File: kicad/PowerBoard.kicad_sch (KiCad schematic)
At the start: 147 parts, among them IC1 LT1910ES8#PBF, IC2 LT1910ES8#PBF, IC3 LT1910ES8#PBF, IC4 LT1910ES8#PBF, IC5 LT1910ES8#PBF, IC7 MAX17541GATB+T, J1 XT90, J10 XT90, J11 XT90, J12 XT90, J13 XT90, J14 DEAN_T, J15 DEAN_T, J16 DEAN_T, J17 DEAN_T, J18 DEAN_T, J19 DEAN_T, J2 DEAN_T, J20 XT60, J21 XT60, J22 XT60, J23 XT60, J24 XT60, J25 XT60, J26 XT60, J27 XT60, J28 XT60, J29 XT60, J3 XT60, J30 XT60, J31 XT60, J32 XT30, J33 XT30, J34 XT30, J35 XT30, J36 XT30, J37 XT30, J38 XT30, J39 XT30, J4 XT30, J40 XT30, J41 XT60, J5 Conn_01x02, J6 XT90, J7 XT90, J8 XT90, J9 XT90, Q1 IRFS7530TRL7PP, Q2 IRFS7437TRLPBF, Q3 IRFS7437TRLPBF, Q4 IRFS7437TRLPBF, Q5 IRFS7437TRLPBF, U1 Pico, U2 INA238, U3 INA238, U4 INA238, U5 INA238, U6 INA238

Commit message: Add first firmware version
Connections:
- net +42V: no longer D20.2 (A)
- net 42_SHUNT: now reaches Q1.4 (D), R1.4
- net 42_SHUNT: now also D20.2 (A)
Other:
- moved on the sheet: D20
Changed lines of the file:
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@@
 	)
 	(junction
-		(at 246.38 44.45)
-		(diameter 0)
-		(color 0 0 0 0)
-	)
-	(junction
 		(at 297.18 101.6)
 		(diameter 0)
@@
 	)
 	(junction
+		(at 38.1 71.12)
+		(diameter 0)
+		(color 0 0 0 0)
+	)
+	(junction
 		(at 93.98 234.95)
 		(diameter 0)
@@
 	)
 	(junction
+		(at 246.38 44.45)
+		(diameter 0)
+		(color 0 0 0 0)
+	)
+	(junction
 		(at 142.24 260.35)
 		(diameter 0)
@@
 	(wire
 		(pts
-			(xy 246.38 31.75) (xy 246.38 34.29)
+			(xy 238.76 36.83) (xy 246.38 36.83)
 		)
 		(stroke
@@
 	(wire
 		(pts
+			(xy 228.6 36.83) (xy 231.14 36.83)
+		)
+		(stroke
+			(width 0)
+			(type default)
+		)
+	)
+	(wire
+		(pts
 			(xy 245.11 120.65) (xy 252.73 120.65)
 		)
@@
 	(wire
 		(pts
-			(xy 246.38 41.91) (xy 246.38 44.45)
-		)
-		(stroke
-			(width 0)
-			(type default)
-		)
-	)
-	(wire
-		(pts
 			(xy 162.56 111.76) (xy 195.58 111.76)
 		)
@@
 	(wire
 		(pts
+			(xy 27.94 71.12) (xy 38.1 71.12)
+		)
+		(stroke
+			(width 0)
+			(type default)
+		)
+	)
+	(wire
+		(pts
 			(xy 118.11 234.95) (xy 118.11 241.3)
 		)
@@
 	(wire
 		(pts
-			(xy 242.57 44.45) (xy 242.57 33.02)
+			(xy 242.57 33.02) (xy 242.57 44.45)
 		)
 		(stroke
@@
 	(wire
 		(pts
+			(xy 246.38 36.83) (xy 246.38 44.45)
+		)
+		(stroke
+			(width 0)
+			(type default)
+		)
+	)
+	(wire
+		(pts
 			(xy 309.88 231.14) (xy 309.88 236.22)
 		)
@@
 	)
 	(rectangle
-		(start 19.05 21.59)
+		(start 13.97 21.59)
 		(end 113.03 86.36)
 		(stroke
@@
 	)
 	(rectangle
-		(start 218.44 21.59)
+		(start 214.63 21.59)
 		(end 332.74 81.28)
 		(stroke
@@
 	(text "5V AUX Switched Power Supply"
 		(exclude_from_sim no)
-		(at 249.428 24.638 0)
+		(at 246.126 24.638 0)
 		(effects
 			(font
@@
 		)
 	)
+	(global_label "42_SHUNT"
+		(shape input)
+		(at 27.94 71.12 180)
+		(fields_autoplaced yes)
+		(effects
+			(font
+				(size 1.27 1.27)
+			)
+			(justify right)
+		)
+		(property "Intersheetrefs" "${INTERSHEET_REFS}"
+			(at 15.3996 71.12 0)
+			(effects
+				(font
+					(size 1.27 1.27)
+				)
+				(justify right)
+				(hide yes)
+			)
+		)
+	)
 	(global_label "ALERT_5"
 		(shape input)
@@
 		)
 	)
+	(global_label "42_SHUNT"
+		(shape input)
+		(at 228.6 36.83 180)
+		(fields_autoplaced yes)
+		(effects
+			(font
+				(size 1.27 1.27)
+			)
+			(justify right)
+		)
+		(property "Intersheetrefs" "${INTERSHEET_REFS}"
+			(at 216.0596 36.83 0)
+			(effects
+				(font
+					(size 1.27 1.27)
+				)
+				(justify right)
+				(hide yes)
+			)
+		)
+	)
 	(global_label "24V_2"
 		(shape input)
@@
 	(symbol
 		(lib_id "Device:D")
-		(at 246.38 38.1 90)
+		(at 234.95 36.83 180)
 		(unit 1)
 		(exclude_from_sim no)
@@
 		(fields_autoplaced yes)
 		(property "Reference" "D20"
-			(at 248.92 36.8299 90)
+			(at 234.95 30.48 0)
 			(effects
 				(font
 					(size 1.27 1.27)
 				)
-				(justify right)
 			)
 		)
 		(property "Value" "D"
-			(at 248.92 39.3699 90)
+			(at 234.95 33.02 0)
 			(effects
 				(font
 					(size 1.27 1.27)
 				)
-				(justify right)
 			)
 		)
 		(property "Footprint" "Diode_SMD:D_1206_3216Metric"
-			(at 246.38 38.1 0)
+			(at 234.95 36.83 0)
 			(effects
 				(font
@@
 		)
 		(property "Datasheet" "~"
-			(at 246.38 38.1 0)
+			(at 234.95 36.83 0)
 			(effects
 				(font
@@
 		)
 		(property "Description" "Diode"
-			(at 246.38 38.1 0)
+			(at 234.95 36.83 0)
 			(effects
 				(font
@@
 		)
 		(property "Sim.Device" "D"
-			(at 246.38 38.1 0)
+			(at 234.95 36.83 0)
 			(effects
 				(font
@@
 		)
 		(property "Sim.Pins" "1=K 2=A"
-			(at 246.38 38.1 0)
+			(at 234.95 36.83 0)
 			(effects
 				(font
@@
 					(unit 1)
 				)
-			)
-		)
-	)
-	(symbol
-		(lib_id "power:+48V")
-		(at 246.38 31.75 0)
-		(unit 1)
-		(exclude_from_sim no)
-		(in_bom yes)
-		(on_board yes)
-		(dnp no)
-		(property "Reference" "#PWR023"
-			(at 246.38 35.56 0)
-			(effects
-				(font
-					(size 1.27 1.27)
-				)
-				(hide yes)
-			)
-		)
-		(property "Value" "+42V"
-			(at 243.84 26.67 0)
-			(effects
-				(font
-					(size 1.27 1.27)
-				)
-				(justify left)
-			)
-		)
-		(property "Footprint" ""
-			(at 246.38 31.75 0)
-			(effects
-				(font
-					(size 1.27 1.27)
-				)
-				(hide yes)
-			)
-		)
-		(property "Datasheet" ""
-			(at 246.38 31.75 0)
-			(effects
-				(font
-					(size 1.27 1.27)
-				)
-				(hide yes)
-			)
-		)
-		(property "Description" "Power symbol creates a global label with name \"+42V\""
-			(at 246.38 31.75 0)
-			(effects
-				(font
-					(size 1.27 1.27)
-				)
-				(hide yes)
-			)
-		)
-		(pin "1"
-		)
-		(instances
-			(project "PowerBoard"
-				(path "/0dc459cd-c845-409c-9d50-e420f03142d8"
-					(reference "#PWR023")
-					(unit 1)
-				)

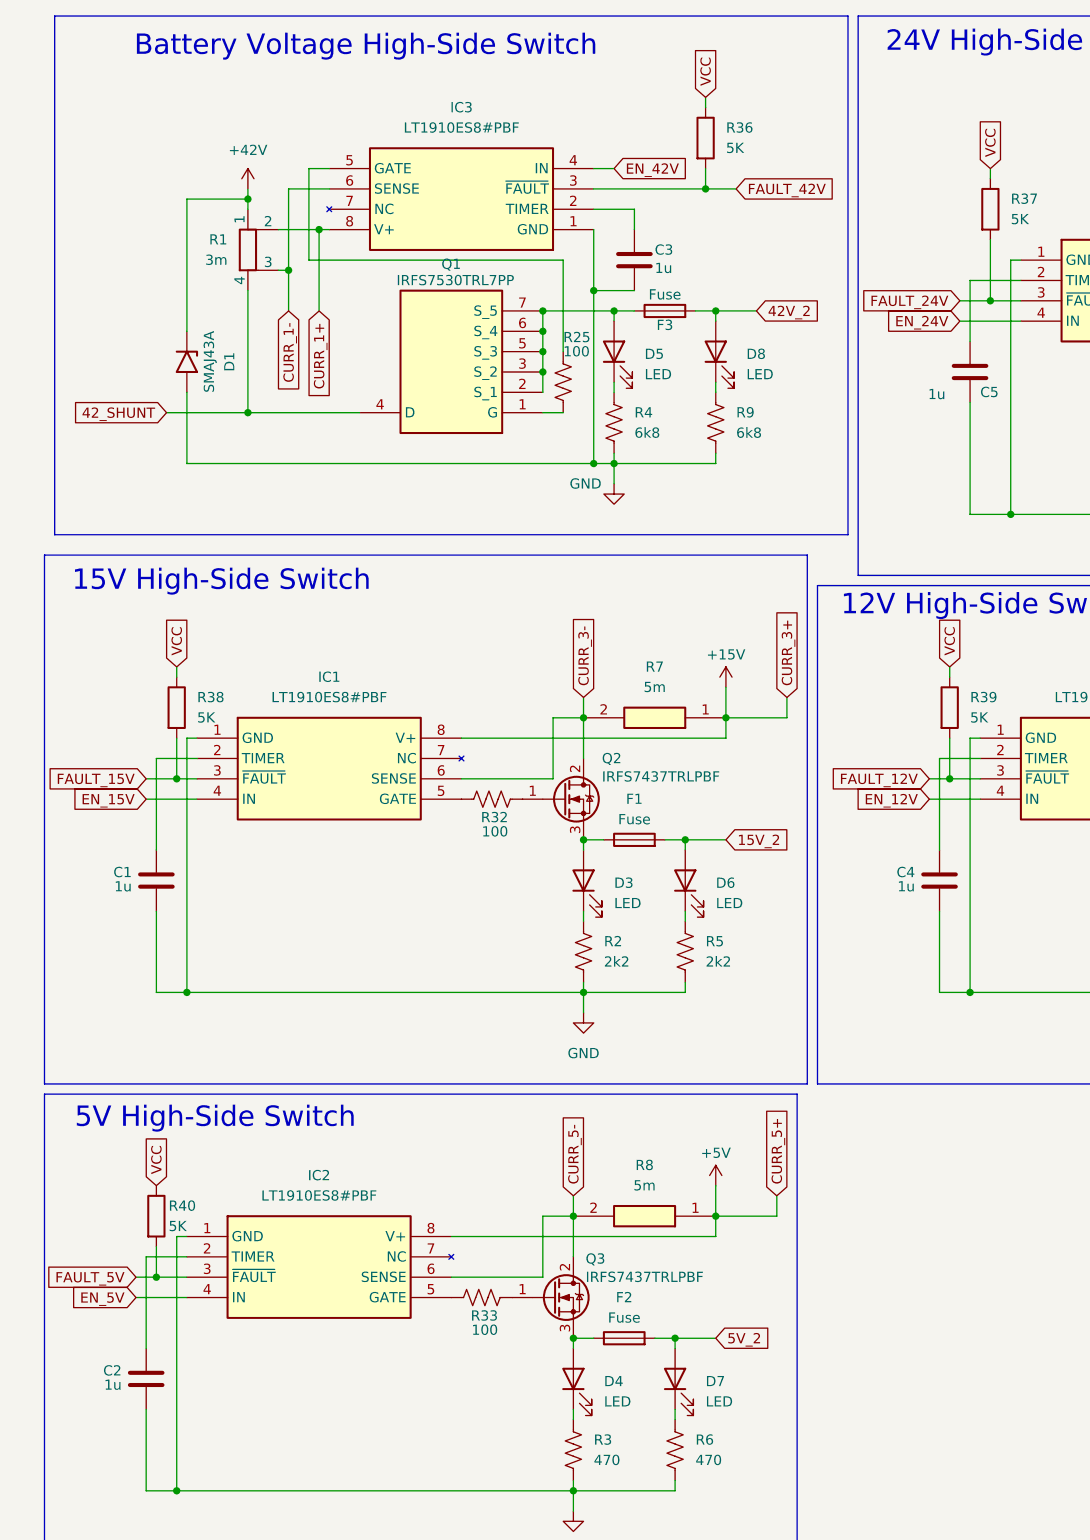
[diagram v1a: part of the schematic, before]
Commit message: Add dV/dt for inrush current limitation on the main power line
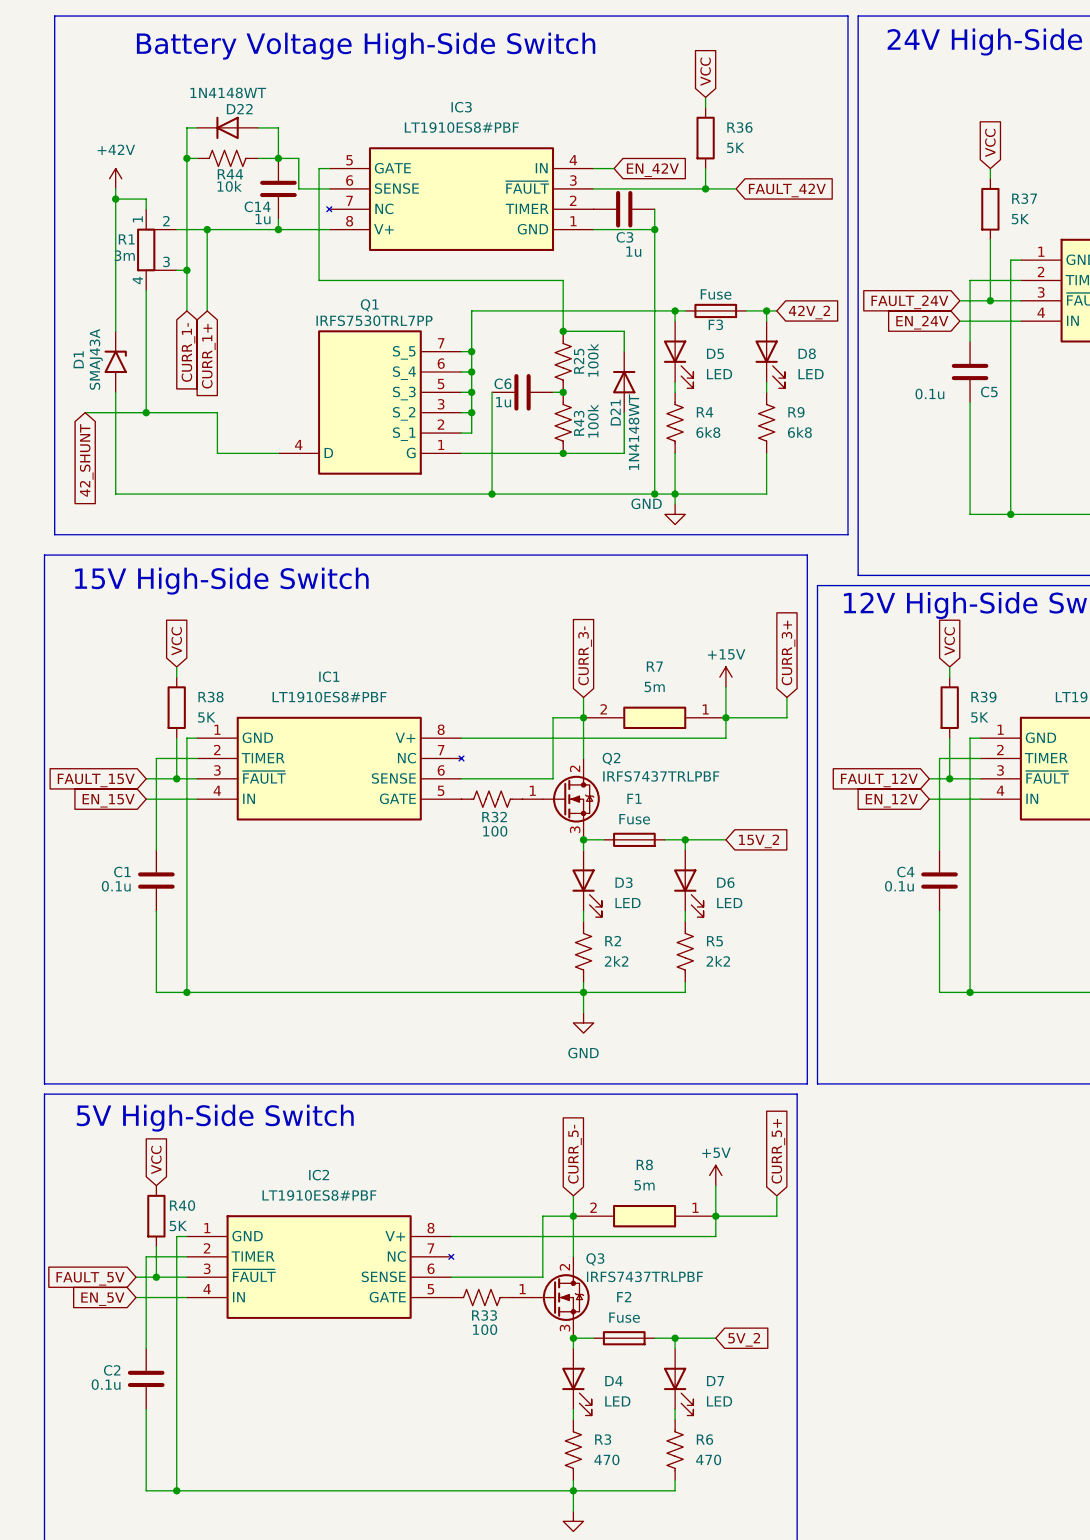
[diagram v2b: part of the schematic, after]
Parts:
- added C14, C6: 1u, Capacitor_SMD:C_0603_1608Metric, symbol Device:C
- added D21, D22: 1N4148WT, Diode_SMD:D_SOD-523, symbol Diode:1N4148WT
- added R43: 100k, Resistor_SMD:R_0603_1608Metric, symbol Device:R_US
- added R44: 10k, Resistor_SMD:R_0603_1608Metric, symbol Device:R_US
- C1, C2, C4, C5: value 1u -> 0.1u
- C10, C11, C12, C3, C7, C8, C9: footprint Capacitor_SMD:C_1206_3216Metric -> Capacitor_SMD:C_0603_1608Metric
- R16, R17, R21: footprint Resistor_SMD:R_1206_3216Metric -> Resistor_SMD:R_0603_1608Metric
- R25: value 100 -> 100k; footprint Resistor_SMD:R_1206_3216Metric -> Resistor_SMD:R_0603_1608Metric
- R4: footprint Resistor_SMD:R_1206_3216Metric -> Capacitor_SMD:C_0603_1608Metric
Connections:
- net CURR_1+: now also C14.2
- net CURR_1-: now also D22.1 (K), R44.1; no longer IC3.6 (SENSE)
- net GND: now also C6.1
- net at R25.1: now also C6.2, R43.1; no longer IC3.5 (GATE)
- net at Q1.1 (G): now also D21.2 (A), R43.2; no longer R25.2
- new net: D21.1 (K), IC3.5 (GATE), R25.2
- new net: C14.1, D22.2 (A), IC3.6 (SENSE), R44.2
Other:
- moved on the sheet: C3, D1, D5, D8, F3, Q1, R1, R25, R4, R9

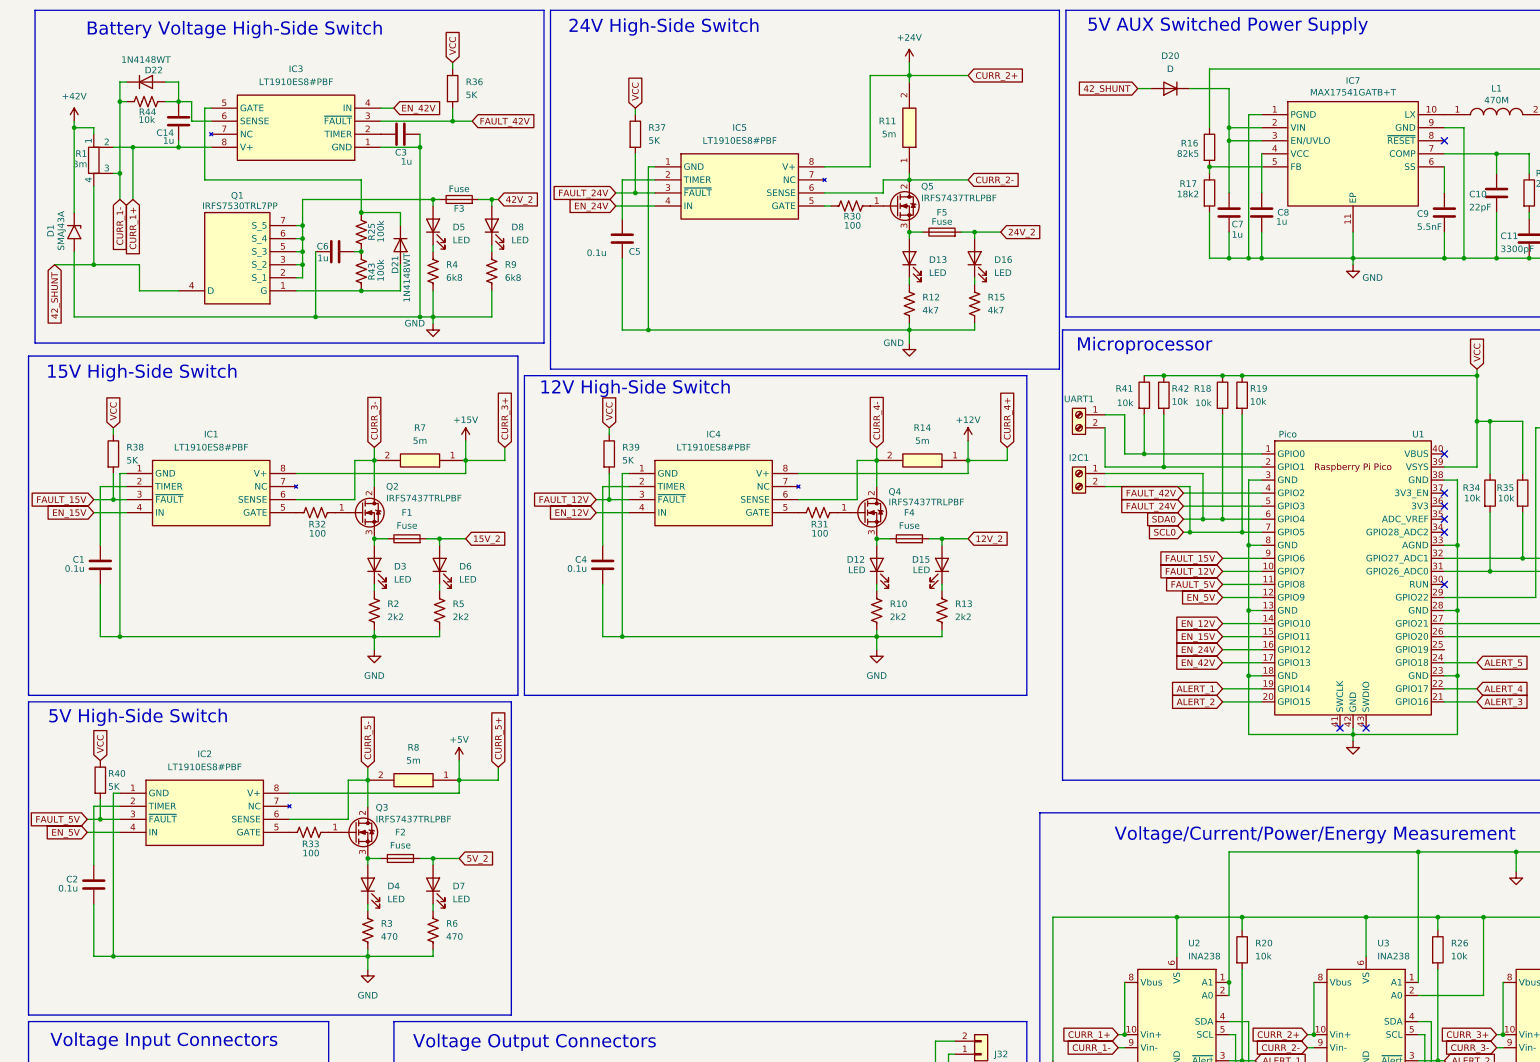
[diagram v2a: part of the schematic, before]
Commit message: finish inrush current limiting
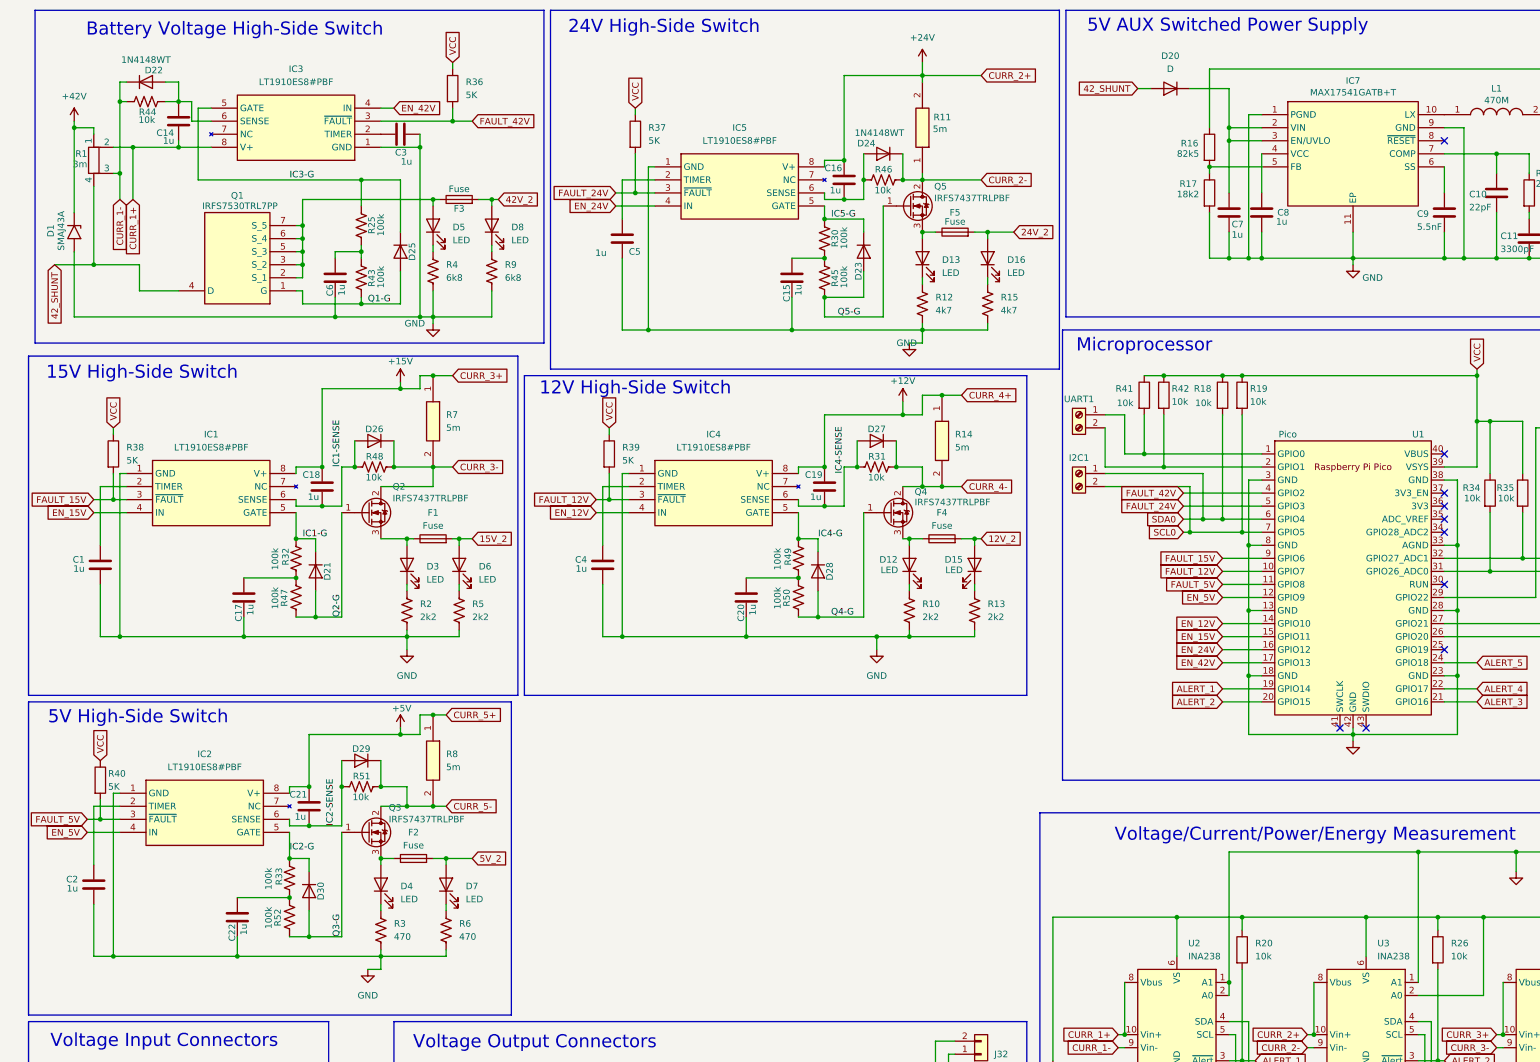
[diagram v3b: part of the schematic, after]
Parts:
- added C15, C16, C17, C18, C19, C20, C21, C22: 1u, Capacitor_SMD:C_0603_1608Metric, symbol Device:C
- added D23, D24, D25, D26, D27, D28, D29, D30: 1N4148WT, Diode_SMD:D_SOD-523, symbol Diode:1N4148WT
- added R45, R47, R49, R50, R52: 100k, Resistor_SMD:R_0603_1608Metric, symbol Device:R_US
- added R46, R48, R51: 10k, Resistor_SMD:R_0603_1608Metric, symbol Device:R_US
- C1, C2, C4, C5: value 0.1u -> 1u; footprint Capacitor_SMD:C_1206_3216Metric -> Capacitor_SMD:C_0603_1608Metric
- R10, R12, R2, R3: footprint Resistor_SMD:R_1206_3216Metric -> Resistor_SMD:R_0603_1608Metric
- R30, R32, R33: value 100 -> 100k; footprint Resistor_SMD:R_1206_3216Metric -> Resistor_SMD:R_0603_1608Metric
- R31: value 100 -> 10k; footprint Resistor_SMD:R_1206_3216Metric -> Resistor_SMD:R_0603_1608Metric
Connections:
- net +12V: now also C19.1
- net +15V: now also C18.1
- net +24V: now also C16.1
- net +5V: now also C21.1
- net CURR_2-: now also D24.1 (K), R46.2; no longer IC5.6 (SENSE)
- net CURR_3-: now also D26.1 (K), R48.2; no longer IC1.6 (SENSE)
- net CURR_4-: now also R31.2, D27.1 (K); no longer IC4.6 (SENSE)
- net CURR_5-: now also D29.1 (K), R51.2; no longer IC2.6 (SENSE)
- net GND: now also C15.1, C17.1, C20.1, C22.1
- net Q1-G: now reaches Q1.1 (G), R43.2
- net Q1-G: now also D25.2 (A); no longer D21.2 (A)
- net at R30.1: now also C15.2, R45.1; no longer IC5.5 (GATE)
- net IC5-G: now reaches R30.2
- net IC5-G: now also IC5.5 (GATE), D23.1 (K); no longer Q5.1 (G)
- net IC3-G: now reaches IC3.5 (GATE), R25.2
- net IC3-G: now also D25.1 (K); no longer D21.1 (K)
- net IC4-G: now reaches IC4.5 (GATE)
- net IC4-G: now also D28.1 (K), R49.2; no longer R31.1
- net IC1-G: now reaches R32.2
- net IC1-G: now also D21.1 (K), IC1.5 (GATE); no longer Q2.1 (G)
- net at R32.1: now also C17.2, R47.1; no longer IC1.5 (GATE)
- net Q4-G: now reaches Q4.1 (G)
- net Q4-G: now also D28.2 (A), R50.2; no longer R31.2
- net at R33.1: now also C22.2, R52.1; no longer IC2.5 (GATE)
- net IC2-G: now reaches R33.2
- net IC2-G: now also IC2.5 (GATE), D30.1 (K); no longer Q3.1 (G)
- new net: C20.2, R49.1, R50.1
- new net: C16.2, D24.2 (A), IC5.6 (SENSE), R46.1
- new net IC1-SENSE: C18.2, D26.2 (A), IC1.6 (SENSE), R48.1
- new net IC2-SENSE: C21.2, D29.2 (A), IC2.6 (SENSE), R51.1
- new net IC4-SENSE: C19.2, D27.2 (A), IC4.6 (SENSE), R31.1
- new net Q2-G: D21.2 (A), Q2.1 (G), R47.2
- new net Q3-G: D30.2 (A), Q3.1 (G), R52.2
- new net Q5-G: D23.2 (A), Q5.1 (G), R45.2
- no-connect marks 9 -> 10
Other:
- moved on the sheet: C6, D12, D13, D15, D16, D3, D4, D6, D7, F1, F2, F4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
